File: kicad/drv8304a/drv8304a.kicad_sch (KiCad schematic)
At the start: 6 parts, among them Q1 CSD18534Q5A, Q2 CSD18534Q5A, Q3 CSD18534Q5A, Q4 CSD18534Q5A, Q5 CSD18534Q5A, Q6 CSD18534Q5A

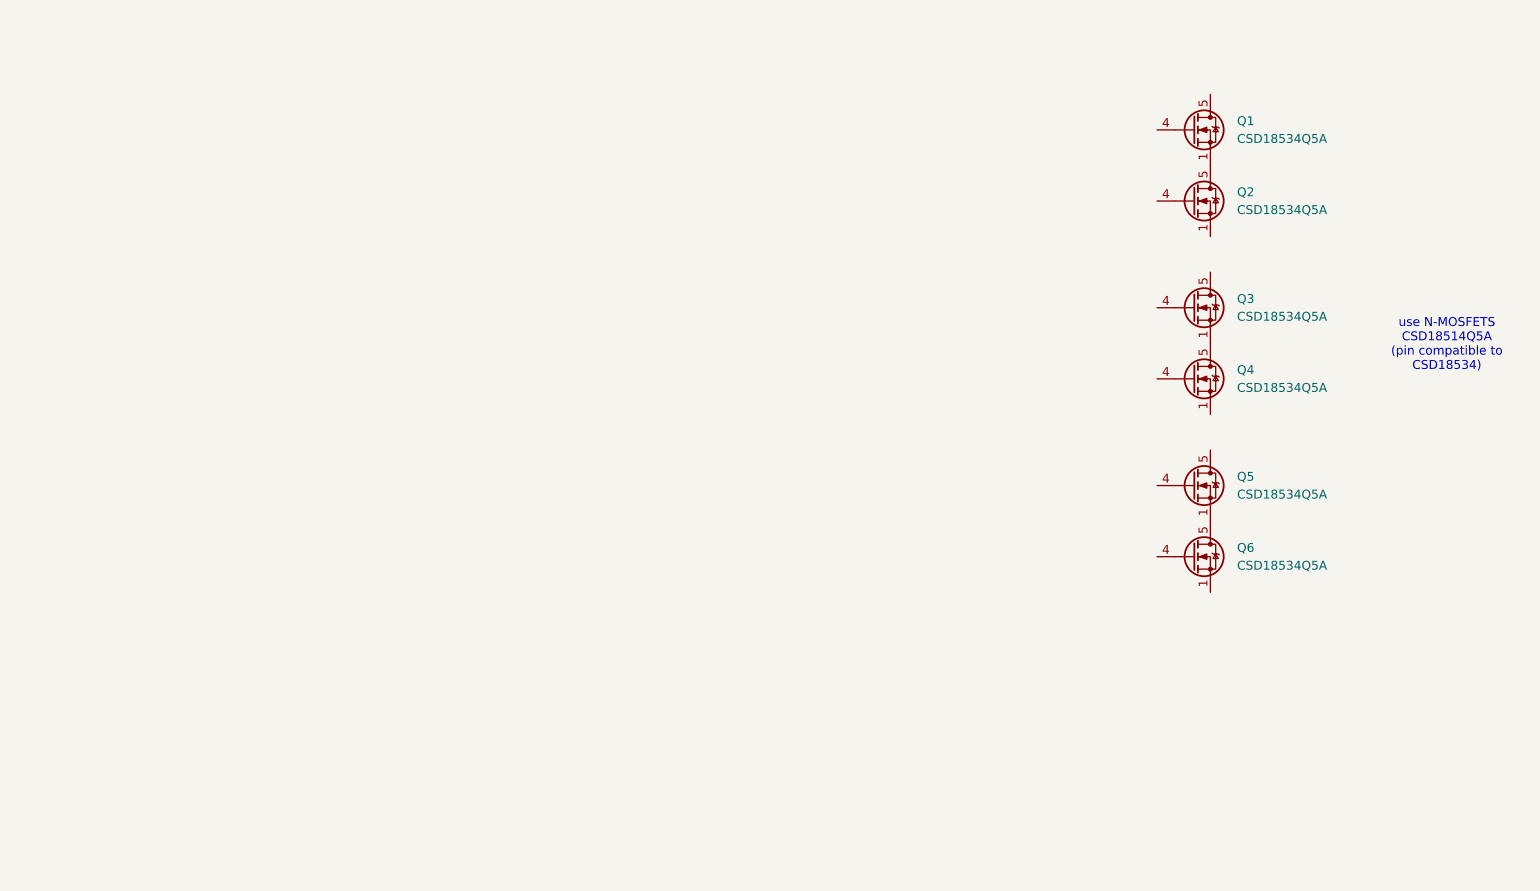
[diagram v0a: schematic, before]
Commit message: DRV8304a schematics done, starting layout
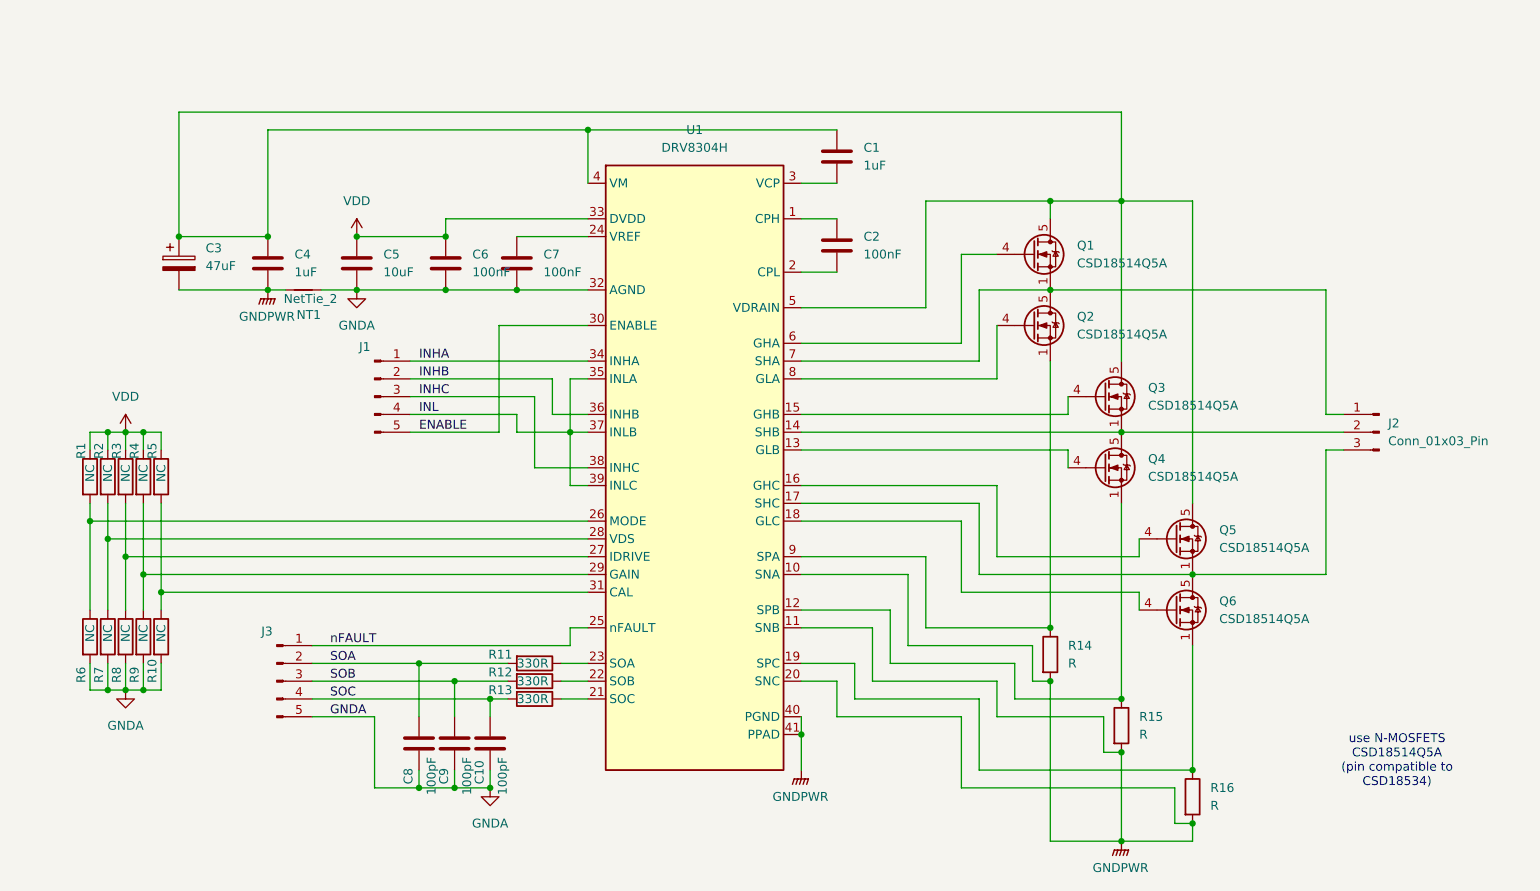
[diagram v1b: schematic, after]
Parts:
- added C1, C4: 1uF, Capacitor_SMD:C_0805_2012Metric_Pad1.18x1.45mm_HandSolder, symbol Device:C
- added C10, C8, C9: 100pF, Capacitor_SMD:C_0603_1608Metric_Pad1.08x0.95mm_HandSolder, symbol Device:C
- added C2, C6, C7: 100nF, Capacitor_SMD:C_0603_1608Metric_Pad1.08x0.95mm_HandSolder, symbol Device:C
- added C3: 47uF, Capacitor_SMD:CP_Elec_6.3x7.7, symbol Device:C_Polarized
- added C5: 10uF, Capacitor_SMD:C_0805_2012Metric_Pad1.18x1.45mm_HandSolder, symbol Device:C
- added J1, J3: Conn_01x05_Pin, Connector_PinHeader_2.54mm:PinHeader_1x05_P2.54mm_Vertical, symbol Connector:Conn_01x05_Pin
- added J2: Conn_01x03_Pin, TerminalBlock_Phoenix:TerminalBlock_Phoenix_MKDS-1,5-3-5.08_1x03_P5.08mm_Horizontal, symbol Connector:Conn_01x03_Pin
- added NT1: NetTie_2, NetTie:NetTie-2_SMD_Pad2.0mm, symbol Device:NetTie_2
- added R1, R10, R2, R3, R4, R5, R6, R7, R8, R9: NC, Resistor_SMD:R_0603_1608Metric_Pad0.98x0.95mm_HandSolder, symbol Device:R
- added R11, R12, R13: 330R, Resistor_SMD:R_0603_1608Metric_Pad0.98x0.95mm_HandSolder, symbol Device:R
- added R14, R15, R16: R, Resistor_SMD:R_2512_6332Metric_Pad1.40x3.35mm_HandSolder, symbol Device:R
- added U1: DRV8304H, Package_DFN_QFN:Texas_RHA0040E_VQFN-40-1EP_6x6mm_P0.5mm_EP3.52x2.62mm, symbol bldc-driver-lib:DRV8304H
- Q1, Q2, Q3, Q4, Q5, Q6: value CSD18534Q5A -> CSD18514Q5A
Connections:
- net at Q4.1 (S), Q4.2 (S), Q4.3 (S): now also R15.1, U1.12 (SPB)
- net at Q4.4 (G): now also U1.13 (GLB)
- net at Q3.1 (S), Q3.2 (S), Q3.3 (S)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: now also J2.2 (Pin_2), U1.14 (SHB)
- net at Q2.1 (S), Q2.2 (S), Q2.3 (S): now also R14.1, U1.9 (SPA)
- net at Q2.4 (G): now also U1.8 (GLA)
- net at Q1.1 (S), Q1.2 (S), Q1.3 (S)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: now also J2.1 (Pin_1), U1.7 (SHA)
- net at Q1.4 (G): now also U1.6 (GHA)
- net at Q1.5 (D): now also Q3.5 (D), Q5.5 (D), C1.1, C3.1, C4.1, U1.4 (VM), U1.5 (VDRAIN)
- net at Q3.4 (G): now also U1.15 (GHB)
- net at Q5.1 (S), Q5.2 (S), Q5.3 (S)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: now also J2.3 (Pin_3), U1.17 (SHC)
- net at Q5.4 (G): now also U1.16 (GHC)
- net at Q6.1 (S), Q6.2 (S), Q6.3 (S): now also R16.1, U1.19 (SPC)
- net at Q6.4 (G): now also U1.18 (GLC)
- new net: R10.1, R5.2, U1.31 (CAL)
- new net: R12.1, U1.22 (SOB)
- new net: C2.1, U1.1 (CPH)
- new net: C2.2, U1.2 (CPL)
- new net: R13.1, U1.21 (SOC)
- new net: R11.1, U1.23 (SOA)
- new net: C7.1, U1.24 (VREF)
- new net: R1.2, R6.1, U1.26 (MODE)
- new net: R3.2, R8.1, U1.27 (IDRIVE)
- new net: R2.2, R7.1, U1.28 (VDS)
- new net: R4.2, R9.1, U1.29 (GAIN)
- new net: C1.2, U1.3 (VCP)
- new net ENABLE: J1.5 (Pin_5), U1.30 (ENABLE)
- new net GNDA: C10.2, C5.2, C6.2, C7.2, C8.2, C9.2, J3.5 (Pin_5), NT1.2, R10.2, R6.2, R7.2, R8.2, R9.2, U1.32 (AGND)
- new net GNDPWR: C3.2, C4.2, NT1.1, R14.2, R15.2, R16.2, U1.10 (SNA), U1.11 (SNB), U1.20 (SNC), U1.40 (PGND), U1.41 (PPAD)
- new net INHA: J1.1 (Pin_1), U1.34 (INHA)
- new net INHB: J1.2 (Pin_2), U1.36 (INHB)
- new net INHC: J1.3 (Pin_3), U1.38 (INHC)
- new net INL: J1.4 (Pin_4), U1.35 (INLA), U1.37 (INLB), U1.39 (INLC)
- new net SOA: C8.1, J3.2 (Pin_2), R11.2
- new net SOB: C9.1, J3.3 (Pin_3), R12.2
- new net SOC: C10.1, J3.4 (Pin_4), R13.2
- new net VDD: C5.1, C6.1, R1.1, R2.1, R3.1, R4.1, R5.1, U1.33 (DVDD)
- new net nFAULT: J3.1 (Pin_1), U1.25 (nFAULT)
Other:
- moved on the sheet: Q1, Q2, Q3, Q4, Q5, Q6

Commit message: some routing
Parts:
- added C11, C12, C13: 1uF, Capacitor_SMD:C_0805_2012Metric_Pad1.18x1.45mm_HandSolder, symbol Device:C
- added J4: Conn_01x02_Pin, Connector_PinHeader_2.54mm:PinHeader_1x02_P2.54mm_Vertical, symbol Connector:Conn_01x02_Pin
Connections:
- net GNDPWR: now also C11.2, C12.2, C13.2, J4.2 (Pin_2)
- net SPB: now reaches Q4.1 (S), Q4.2 (S), Q4.3 (S), R15.1, U1.12 (SPB)
- net GLB: now reaches Q4.4 (G), U1.13 (GLB)
- net SHB: now reaches J2.2 (Pin_2), Q3.1 (S), Q3.2 (S), Q3.3 (S), Q4.5 (D), U1.14 (SHB)
- net GHB: now reaches Q3.4 (G), U1.15 (GHB)
- net GHC: now reaches Q5.4 (G), U1.16 (GHC)
- net SHC: now reaches J2.3 (Pin_3), Q5.1 (S), Q5.2 (S), Q5.3 (S), Q6.5 (D), U1.17 (SHC)
- net GLC: now reaches Q6.4 (G), U1.18 (GLC)
- net SPC: now reaches Q6.1 (S), Q6.2 (S), Q6.3 (S), R16.1, U1.19 (SPC)
- net VM: now reaches C1.1, C3.1, C4.1, Q1.5 (D), Q3.5 (D), Q5.5 (D), U1.4 (VM), U1.5 (VDRAIN)
- net VM: now also C11.1, C12.1, C13.1, J4.1 (Pin_1)
- net GHA: now reaches Q1.4 (G), U1.6 (GHA)
- net SHA: now reaches J2.1 (Pin_1), Q1.1 (S), Q1.2 (S), Q1.3 (S), Q2.5 (D), U1.7 (SHA)
- net GLA: now reaches Q2.4 (G), U1.8 (GLA)
- net SPA: now reaches Q2.1 (S), Q2.2 (S), Q2.3 (S), R14.1, U1.9 (SPA)
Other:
- note added: "cap for every FET"

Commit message: FETS routed
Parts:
- J4: footprint Connector_PinHeader_2.54mm:PinHeader_1x02_P2.54mm_Vertical -> TerminalBlock_Phoenix:TerminalBlock_Phoenix_MKDS-1,5-2_1x02_P5.00mm_Horizontal
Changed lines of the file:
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@@
 			)
 		)
-		(property "Footprint" "Connector_PinHeader_2.54mm:PinHeader_1x02_P2.54mm_Vertical"
+		(property "Footprint" "TerminalBlock_Phoenix:TerminalBlock_Phoenix_MKDS-1,5-2_1x02_P5.00mm_Horizontal"
 			(at 66.04 63.5 0)
 			(effects

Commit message: lots routed
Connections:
- net VDD: now also C7.1, U1.24 (VREF)
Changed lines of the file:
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@@
 	)
 	(junction
+		(at 129.54 60.96)
+		(diameter 0)
+		(color 0 0 0 0)
+	)
+	(junction
 		(at 215.9 147.32)
 		(diameter 0)
@@
 	(wire
 		(pts
+			(xy 119.38 60.96) (xy 129.54 60.96)
+		)
+		(stroke
+			(width 0)
+			(type default)
+		)
+	)
+	(wire
+		(pts
 			(xy 71.12 66.04) (xy 76.2 66.04)
 		)
@@
 		(on_board yes)
 		(dnp no)
-		(fields_autoplaced yes)
 		(property "Reference" "C7"
 			(at 133.35 63.4999 0)
@@
 		(on_board yes)
 		(dnp no)
-		(fields_autoplaced yes)
 		(property "Reference" "C2"
 			(at 179.07 60.9599 0)

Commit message: DRV8304a done
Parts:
- R1, R10, R2, R3, R4, R5, R6, R7, R8, R9: value NC -> DNP
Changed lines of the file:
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@@
 			)
 		)
-		(property "Value" "NC"
-			(at 78.74 118.8719 90)
+		(property "Value" "DNP"
+			(at 78.74 119.8879 90)
 			(effects
 				(font
@@
 			)
 		)
-		(property "Value" "NC"
-			(at 68.58 96.0119 90)
+		(property "Value" "DNP"
+			(at 68.58 97.0279 90)
 			(effects
 				(font
@@
 			)
 		)
-		(property "Value" "NC"
-			(at 71.12 118.8719 90)
+		(property "Value" "DNP"
+			(at 71.12 119.8879 90)
 			(effects
 				(font
@@
 			)
 		)
-		(property "Value" "NC"
-			(at 76.2 96.0119 90)
+		(property "Value" "DNP"
+			(at 76.2 97.0279 90)
 			(effects
 				(font
@@
 			)
 		)
-		(property "Value" "NC"
-			(at 78.74 96.0119 90)
+		(property "Value" "DNP"
+			(at 78.74 97.0279 90)
 			(effects
 				(font
@@
 			)
 		)
-		(property "Value" "NC"
-			(at 76.2 118.8719 90)
+		(property "Value" "DNP"
+			(at 76.2 119.8879 90)
 			(effects
 				(font
@@
 			)
 		)
-		(property "Value" "NC"
-			(at 68.58 118.8719 90)
+		(property "Value" "DNP"
+			(at 68.58 119.8879 90)
 			(effects
 				(font
@@
 			)
 		)
-		(property "Value" "NC"
-			(at 71.12 96.0119 90)
+		(property "Value" "DNP"
+			(at 71.12 97.0279 90)
 			(effects
 				(font
@@
 			)
 		)
-		(property "Value" "NC"
-			(at 73.66 118.8719 90)
+		(property "Value" "DNP"
+			(at 73.66 119.8879 90)
 			(effects
 				(font
@@
 			)
 		)
-		(property "Value" "NC"
-			(at 73.66 96.0119 90)
+		(property "Value" "DNP"
+			(at 73.66 97.0279 90)
 			(effects
 				(font
